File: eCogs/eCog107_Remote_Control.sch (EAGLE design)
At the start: 7 parts, among them T1 MMBT3904LT1G, T3 MMBT3904LT1G, U1 PNA460XM

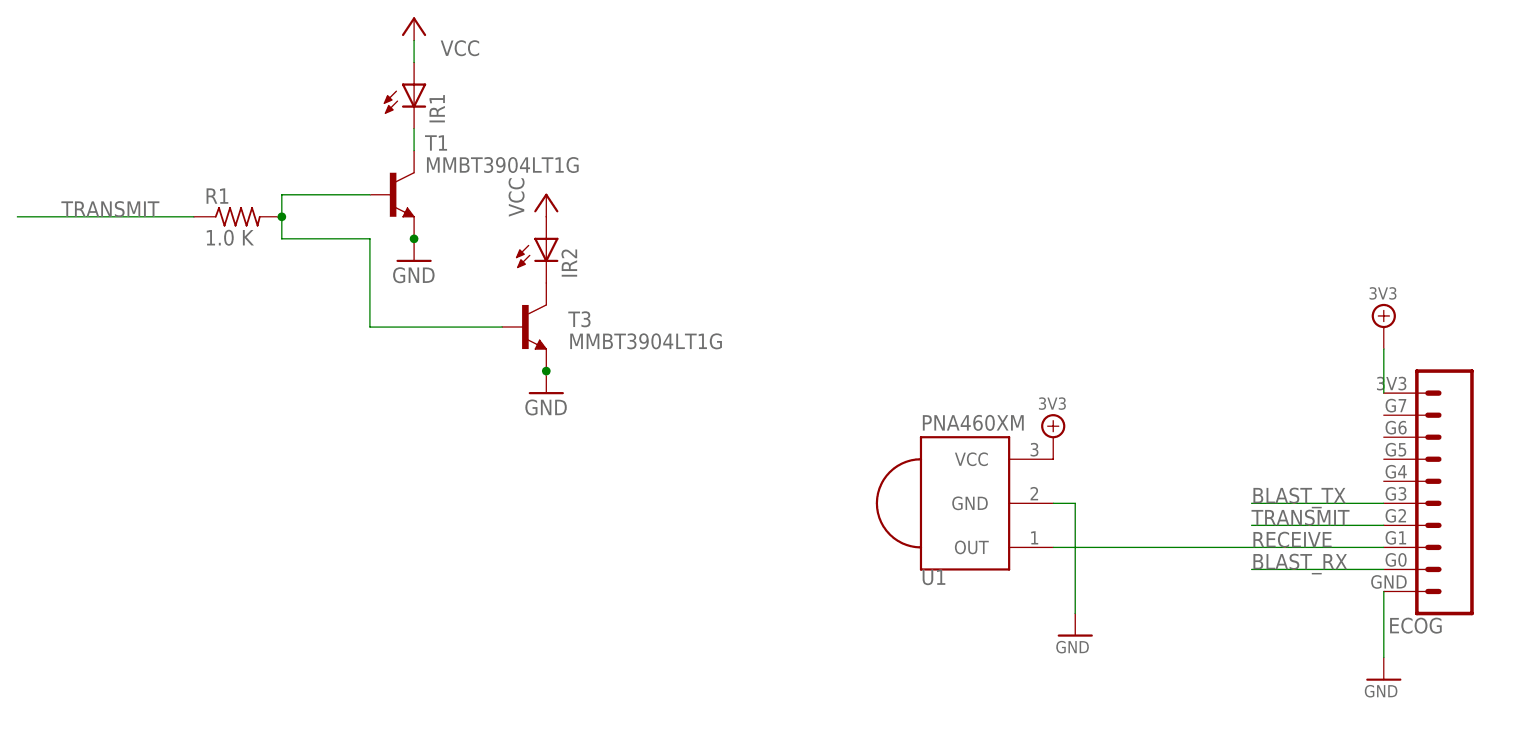
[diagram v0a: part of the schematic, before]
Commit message: Update Remote Control Design
Put the transmit PWM pin on XC4 for greater compatibility.
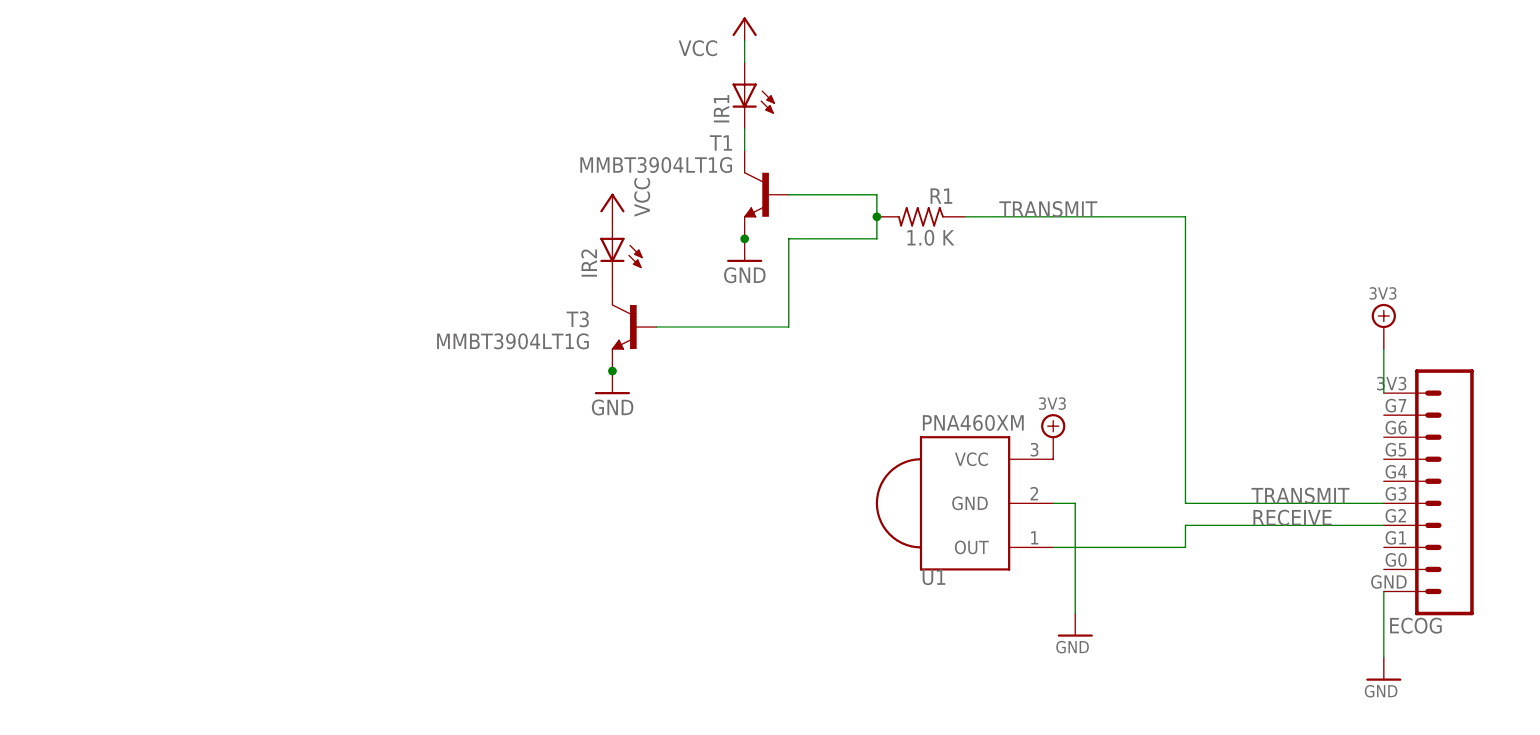
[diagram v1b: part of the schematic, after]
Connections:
- removed net BLAST_RX: ECOG.G0
- removed net BLAST_TX: ECOG.G3
- net RECEIVE: now also ECOG.G2; no longer ECOG.G1
- net TRANSMIT: now also ECOG.G3; no longer ECOG.G2
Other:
- moved on the sheet: IR1, IR2, R1, T1, T3
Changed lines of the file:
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@@
 <instance part="3V3_PWR2" gate="A" x="177.8" y="134.62"/>
 <instance part="GND2" gate="A" x="180.34" y="111.76"/>
-<instance part="GND6" gate="1" x="119.38" y="139.7"/>
-<instance part="P+4" gate="VCC" x="119.38" y="162.56"/>
-<instance part="GND8" gate="1" x="104.14" y="154.94"/>
-<instance part="P+7" gate="VCC" x="104.14" y="182.88" smashed="yes">
-<attribute name="VALUE" x="111.76" y="180.34" size="1.778" layer="96" rot="R180"/>
+<instance part="GND6" gate="1" x="127" y="139.7" rot="MR0"/>
+<instance part="P+4" gate="VCC" x="127" y="162.56" rot="MR0"/>
+<instance part="GND8" gate="1" x="142.24" y="154.94" rot="MR0"/>
+<instance part="P+7" gate="VCC" x="142.24" y="182.88" smashed="yes" rot="MR0">
+<attribute name="VALUE" x="134.62" y="180.34" size="1.778" layer="96" rot="MR180"/>
 </instance>
-<instance part="R1" gate="G$1" x="83.82" y="160.02">
-<attribute name="DIGIKEY" x="83.82" y="160.02" size="1.778" layer="96" display="off"/>
+<instance part="R1" gate="G$1" x="162.56" y="160.02" rot="MR0">
+<attribute name="DIGIKEY" x="162.56" y="160.02" size="1.778" layer="96" rot="MR0" display="off"/>
 </instance>
-<instance part="T1" gate="G$1" x="101.6" y="162.56" smashed="yes">
-<attribute name="NAME" x="105.41" y="167.64" size="1.778" layer="95"/>
-<attribute name="VALUE" x="105.41" y="165.1" size="1.778" layer="96"/>
-<attribute name="DIGIKEY" x="101.6" y="162.56" size="1.778" layer="96" display="off"/>
+<instance part="T1" gate="G$1" x="144.78" y="162.56" smashed="yes" rot="MR0">
+<attribute name="NAME" x="140.97" y="167.64" size="1.778" layer="95" rot="MR0"/>
+<attribute name="VALUE" x="140.97" y="165.1" size="1.778" layer="96" rot="MR0"/>
+<attribute name="DIGIKEY" x="144.78" y="162.56" size="1.778" layer="96" rot="MR0" display="off"/>
 </instance>
-<instance part="T3" gate="G$1" x="116.84" y="147.32" smashed="yes">
-<attribute name="NAME" x="121.92" y="147.32" size="1.778" layer="95"/>
-<attribute name="VALUE" x="121.92" y="144.78" size="1.778" layer="96"/>
-<attribute name="DIGIKEY" x="116.84" y="147.32" size="1.778" layer="96" display="off"/>
+<instance part="T3" gate="G$1" x="129.54" y="147.32" smashed="yes" rot="MR0">
+<attribute name="NAME" x="124.46" y="147.32" size="1.778" layer="95" rot="MR0"/>
+<attribute name="VALUE" x="124.46" y="144.78" size="1.778" layer="96" rot="MR0"/>
+<attribute name="DIGIKEY" x="129.54" y="147.32" size="1.778" layer="96" rot="MR0" display="off"/>
 </instance>
-<instance part="IR1" gate="G$1" x="104.14" y="175.26">
-<attribute name="DIGIKEY" x="104.14" y="175.26" size="1.778" layer="96" display="off"/>
+<instance part="IR1" gate="G$1" x="142.24" y="175.26" rot="MR0">
+<attribute name="DIGIKEY" x="142.24" y="175.26" size="1.778" layer="96" rot="MR0" display="off"/>
 </instance>
-<instance part="IR2" gate="G$1" x="119.38" y="157.48">
-<attribute name="DIGIKEY" x="119.38" y="157.48" size="1.778" layer="96" display="off"/>
+<instance part="IR2" gate="G$1" x="127" y="157.48" rot="MR0">
+<attribute name="DIGIKEY" x="127" y="157.48" size="1.778" layer="96" rot="MR0" display="off"/>
 </instance>
 </instances>
@@
 </segment>
 <segment>
-<wire x1="104.14" y1="177.8" x2="104.14" y2="180.34" width="0.1524" layer="91"/>
+<wire x1="142.24" y1="177.8" x2="142.24" y2="180.34" width="0.1524" layer="91"/>
 <pinref part="P+7" gate="VCC" pin="VCC"/>
 <pinref part="IR1" gate="G$1" pin="A"/>
@@
 <pinref part="GND6" gate="1" pin="GND"/>
 <pinref part="T3" gate="G$1" pin="E"/>
-<junction x="119.38" y="142.24"/>
+<junction x="127" y="142.24"/>
 <pinref part="T3" gate="G$1" pin="E"/>
 </segment>
@@
 <pinref part="GND8" gate="1" pin="GND"/>
 <pinref part="T1" gate="G$1" pin="E"/>
-<junction x="104.14" y="157.48"/>
+<junction x="142.24" y="157.48"/>
 <pinref part="T1" gate="G$1" pin="E"/>
 </segment>
@@
 <net name="TRANSMIT" class="0">
 <segment>
-<pinref part="ECOG" gate="ECOG_GENERAL" pin="G2"/>
-<wire x1="215.9" y1="124.46" x2="200.66" y2="124.46" width="0.2032" layer="91"/>
-<label x="200.66" y="124.46" size="1.778" layer="95"/>
-</segment>
-<segment>
+<pinref part="ECOG" gate="ECOG_GENERAL" pin="G3"/>
+<wire x1="215.9" y1="127" x2="193.04" y2="127" width="0.2032" layer="91"/>
+<label x="200.66" y="127" size="1.778" layer="95"/>
+<wire x1="193.04" y1="127" x2="193.04" y2="160.02" width="0.2032" layer="91"/>
 <pinref part="R1" gate="G$1" pin="1"/>
-<wire x1="78.74" y1="160.02" x2="58.42" y2="160.02" width="0.2032" layer="91"/>
-<label x="63.5" y="160.02" size="1.778" layer="95"/>
-</segment>
-</net>
-<net name="RECEIVE" class="0">
-<segment>
-<pinref part="ECOG" gate="ECOG_GENERAL" pin="G1"/>
-<label x="200.66" y="121.92" size="1.778" layer="95"/>
-<pinref part="U1" gate="G$1" pin="OUT"/>
-<wire x1="177.8" y1="121.92" x2="215.9" y2="121.92" width="0.2032" layer="91"/>
-</segment>
-</net>
-<net name="BLAST_RX" class="0">
-<segment>
-<pinref part="ECOG" gate="ECOG_GENERAL" pin="G0"/>
-<wire x1="215.9" y1="119.38" x2="200.66" y2="119.38" width="0.2032" layer="91"/>
-<label x="200.66" y="119.38" size="1.778" layer="95"/>
-</segment>
-</net>
-<net name="BLAST_TX" class="0">
-<segment>
-<pinref part="ECOG" gate="ECOG_GENERAL" pin="G3"/>
-<wire x1="215.9" y1="127" x2="200.66" y2="127" width="0.2032" layer="91"/>
-<label x="200.66" y="127" size="1.778" layer="95"/>
+<wire x1="167.64" y1="160.02" x2="193.04" y2="160.02" width="0.2032" layer="91"/>
+<label x="182.88" y="160.02" size="1.778" layer="95" rot="MR0"/>
 </segment>
 </net>
@@
 <net name="N$7" class="0">
 <segment>
-<wire x1="104.14" y1="170.18" x2="104.14" y2="167.64" width="0.1524" layer="91"/>
+<wire x1="142.24" y1="170.18" x2="142.24" y2="167.64" width="0.1524" layer="91"/>
 <pinref part="T1" gate="G$1" pin="C"/>
 <pinref part="IR1" gate="G$1" pin="C"/>
@@
 <net name="N$10" class="0">
 <segment>
-<wire x1="114.3" y1="147.32" x2="99.06" y2="147.32" width="0.1524" layer="91"/>
-<wire x1="99.06" y1="147.32" x2="99.06" y2="157.48" width="0.1524" layer="91"/>
-<wire x1="88.9" y1="162.56" x2="99.06" y2="162.56" width="0.1524" layer="91"/>
-<wire x1="99.06" y1="157.48" x2="88.9" y2="157.48" width="0.1524" layer="91"/>
-<wire x1="88.9" y1="157.48" x2="88.9" y2="160.02" width="0.1524" layer="91"/>
+<wire x1="132.08" y1="147.32" x2="147.32" y2="147.32" width="0.1524" layer="91"/>
+<wire x1="147.32" y1="147.32" x2="147.32" y2="157.48" width="0.1524" layer="91"/>
+<wire x1="157.48" y1="162.56" x2="147.32" y2="162.56" width="0.1524" layer="91"/>
+<wire x1="147.32" y1="157.48" x2="157.48" y2="157.48" width="0.1524" layer="91"/>
+<wire x1="157.48" y1="157.48" x2="157.48" y2="160.02" width="0.1524" layer="91"/>
 <pinref part="T1" gate="G$1" pin="B"/>
 <pinref part="T3" gate="G$1" pin="B"/>
 <pinref part="R1" gate="G$1" pin="2"/>
-<wire x1="88.9" y1="160.02" x2="88.9" y2="162.56" width="0.1524" layer="91"/>
-<junction x="88.9" y="160.02"/>
+<wire x1="157.48" y1="160.02" x2="157.48" y2="162.56" width="0.1524" layer="91"/>
+<junction x="157.48" y="160.02"/>
 </segment>
 </net>
+<net name="RECEIVE" class="0">
+<segment>
+<pinref part="U1" gate="G$1" pin="OUT"/>
+<wire x1="177.8" y1="121.92" x2="193.04" y2="121.92" width="0.1524" layer="91"/>
+<wire x1="193.04" y1="121.92" x2="193.04" y2="124.46" width="0.1524" layer="91"/>
+<pinref part="ECOG" gate="ECOG_GENERAL" pin="G2"/>
+<wire x1="193.04" y1="124.46" x2="215.9" y2="124.46" width="0.1524" layer="91"/>
+<label x="200.66" y="124.46" size="1.778" layer="95"/>
+</segment>
+</net>

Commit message: Updated to latest eCog Library
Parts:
- ECOG: value ECOG_GENERAL_ROWECOG_GENERAL_SMD -> ECOG_GENERAL_ROWSURFACEMOUNT; device eCogs:ECOG_GENERAL_ROWECOG_GENERAL_SMD -> eCogs:ECOG_GENERAL_ROWSURFACEMOUNT
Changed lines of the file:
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@@
 <grid distance="0.1" unitdist="inch" unit="inch" style="lines" multiple="1" display="no" altdistance="0.01" altunitdist="inch" altunit="inch"/>
 <layers>
-<layer number="1" name="Top" color="4" fill="1" visible="no" active="no"/>
-<layer number="2" name="Route2" color="1" fill="3" visible="no" active="no"/>
-<layer number="3" name="Route3" color="4" fill="3" visible="no" active="no"/>
-<layer number="4" name="Route4" color="1" fill="4" visible="no" active="no"/>
-<layer number="13" name="Route13" color="4" fill="5" visible="no" active="no"/>
-<layer number="14" name="Route14" color="1" fill="6" visible="no" active="no"/>
-<layer number="15" name="Route15" color="4" fill="6" visible="no" active="no"/>
-<layer number="16" name="Bottom" color="1" fill="1" visible="no" active="no"/>
-<layer number="17" name="Pads" color="2" fill="1" visible="no" active="no"/>
-<layer number="18" name="Vias" color="2" fill="1" visible="no" active="no"/>
-<layer number="19" name="Unrouted" color="6" fill="1" visible="no" active="no"/>
-<layer number="20" name="Dimension" color="15" fill="1" visible="no" active="no"/>
-<layer number="21" name="tPlace" color="16" fill="1" visible="no" active="no"/>
-<layer number="22" name="bPlace" color="14" fill="1" visible="no" active="no"/>
-<layer number="23" name="tOrigins" color="15" fill="1" visible="no" active="no"/>
-<layer number="24" name="bOrigins" color="15" fill="1" visible="no" active="no"/>
-<layer number="25" name="tNames" color="16" fill="1" visible="no" active="no"/>
-<layer number="26" name="bNames" color="7" fill="1" visible="no" active="no"/>
-<layer number="27" name="tValues" color="7" fill="1" visible="no" active="no"/>
-<layer number="28" name="bValues" color="7" fill="1" visible="no" active="no"/>
+<layer number="1" name="Top" color="4" fill="1" visible="yes" active="no"/>
+<layer number="2" name="Route2" color="1" fill="3" visible="yes" active="no"/>
+<layer number="3" name="Route3" color="4" fill="3" visible="yes" active="no"/>
+<layer number="4" name="Route4" color="1" fill="4" visible="yes" active="no"/>
+<layer number="13" name="Route13" color="4" fill="5" visible="yes" active="no"/>
+<layer number="14" name="Route14" color="1" fill="6" visible="yes" active="no"/>
+<layer number="15" name="Route15" color="4" fill="6" visible="yes" active="no"/>
+<layer number="16" name="Bottom" color="1" fill="1" visible="yes" active="no"/>
+<layer number="17" name="Pads" color="2" fill="1" visible="yes" active="no"/>
+<layer number="18" name="Vias" color="2" fill="1" visible="yes" active="no"/>
+<layer number="19" name="Unrouted" color="6" fill="1" visible="yes" active="no"/>
+<layer number="20" name="Dimension" color="15" fill="1" visible="yes" active="no"/>
+<layer number="21" name="tPlace" color="16" fill="1" visible="yes" active="no"/>
+<layer number="22" name="bPlace" color="14" fill="1" visible="yes" active="no"/>
+<layer number="23" name="tOrigins" color="15" fill="1" visible="yes" active="no"/>
+<layer number="24" name="bOrigins" color="15" fill="1" visible="yes" active="no"/>
+<layer number="25" name="tNames" color="16" fill="1" visible="yes" active="no"/>
+<layer number="26" name="bNames" color="7" fill="1" visible="yes" active="no"/>
+<layer number="27" name="tValues" color="7" fill="1" visible="yes" active="no"/>
+<layer number="28" name="bValues" color="7" fill="1" visible="yes" active="no"/>
 <layer number="29" name="tStop" color="7" fill="3" visible="no" active="no"/>
 <layer number="30" name="bStop" color="7" fill="6" visible="no" active="no"/>
@@
 <layer number="35" name="tGlue" color="7" fill="4" visible="no" active="no"/>
 <layer number="36" name="bGlue" color="7" fill="5" visible="no" active="no"/>
-<layer number="37" name="tTest" color="7" fill="1" visible="no" active="no"/>
-<layer number="38" name="bTest" color="7" fill="1" visible="no" active="no"/>
+<layer number="37" name="tTest" color="7" fill="1" visible="yes" active="no"/>
+<layer number="38" name="bTest" color="7" fill="1" visible="yes" active="no"/>
 <layer number="39" name="tKeepout" color="4" fill="11" visible="no" active="no"/>
 <layer number="40" name="bKeepout" color="1" fill="11" visible="no" active="no"/>
@@
 <layer number="44" name="Drills" color="7" fill="1" visible="no" active="no"/>
 <layer number="45" name="Holes" color="7" fill="1" visible="no" active="no"/>
-<layer number="46" name="Milling" color="3" fill="1" visible="no" active="no"/>
-<layer number="47" name="Measures" color="7" fill="1" visible="no" active="no"/>
-<layer number="48" name="Document" color="7" fill="1" visible="no" active="no"/>
-<layer number="49" name="Reference" color="7" fill="1" visible="no" active="no"/>
-<layer number="50" name="dxf" color="7" fill="1" visible="no" active="no"/>
-<layer number="51" name="tDocu" color="6" fill="1" visible="no" active="no"/>
-<layer number="52" name="bDocu" color="7" fill="1" visible="no" active="no"/>
-<layer number="53" name="tGND_GNDA" color="7" fill="9" visible="no" active="no"/>
-<layer number="54" name="bGND_GNDA" color="1" fill="9" visible="no" active="no"/>
-<layer number="56" name="wert" color="3" fill="1" visible="no" active="no"/>
-<layer number="57" name="tCAD" color="7" fill="1" visible="no" active="no"/>
-<layer number="59" name="tCarbon" color="7" fill="1" visible="no" active="no"/>
-<layer number="60" name="bCarbon" color="7" fill="1" visible="no" active="no"/>
+<layer number="46" name="Milling" color="3" fill="1" visible="yes" active="no"/>
+<layer number="47" name="Measures" color="7" fill="1" visible="yes" active="no"/>
+<layer number="48" name="Document" color="7" fill="1" visible="yes" active="no"/>
+<layer number="49" name="Reference" color="7" fill="1" visible="yes" active="no"/>
+<layer number="50" name="dxf" color="7" fill="1" visible="yes" active="no"/>
+<layer number="51" name="tDocu" color="6" fill="1" visible="yes" active="no"/>
+<layer number="52" name="bDocu" color="7" fill="1" visible="yes" active="no"/>
+<layer number="53" name="tGND_GNDA" color="7" fill="9" visible="yes" active="no"/>
+<layer number="54" name="bGND_GNDA" color="1" fill="9" visible="yes" active="no"/>
+<layer number="56" name="wert" color="3" fill="1" visible="yes" active="no"/>
+<layer number="57" name="tCAD" color="7" fill="1" visible="yes" active="no"/>
+<layer number="59" name="tCarbon" color="7" fill="1" visible="yes" active="no"/>
+<layer number="60" name="bCarbon" color="7" fill="1" visible="yes" active="no"/>
 <layer number="90" name="Modules" color="7" fill="1" visible="yes" active="yes"/>
 <layer number="91" name="Nets" color="2" fill="1" visible="yes" active="yes"/>
@@
 <parts>
 <part name="FRAME1" library="frames" deviceset="A3L-LOC" device=""/>
-<part name="ECOG" library="eCogs" deviceset="ECOG_GENERAL_ROW" device="ECOG_GENERAL_SMD" value="ECOG_GENERAL_ROWECOG_GENERAL_SMD"/>
+<part name="ECOG" library="eCogs" deviceset="ECOG_GENERAL_ROW" device="SURFACEMOUNT" value="ECOG_GENERAL_ROWSURFACEMOUNT"/>
 <part name="3V3_PWR1" library="eCogs" deviceset="3V3" device=""/>
 <part name="GND1" library="eCogs" deviceset="GND" device=""/>
